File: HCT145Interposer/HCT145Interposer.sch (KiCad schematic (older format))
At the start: 8 parts, among them J1 Conn_01x01, J3 Header, J7 FORWARD, J8 REVERSE, U1 74HCT125, U2 74LVC245

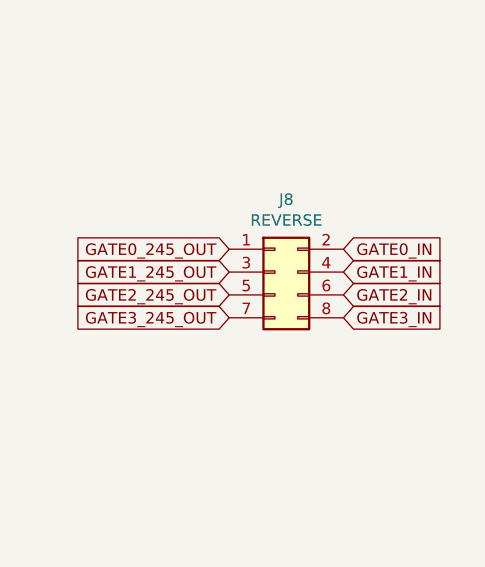
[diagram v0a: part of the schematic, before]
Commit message: Quick fix to HCT145 interposer. Reverse direction was outputting to wrong pins.
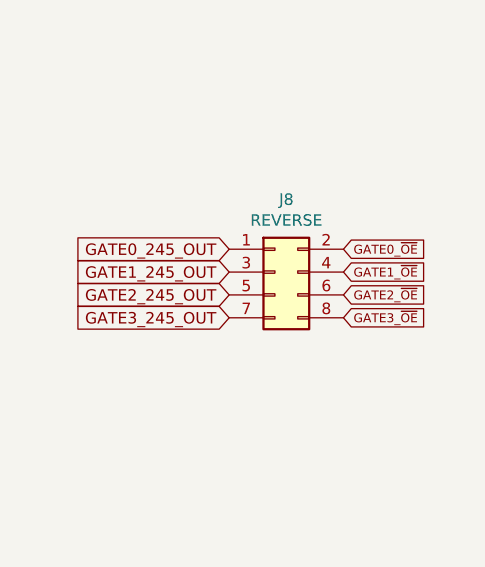
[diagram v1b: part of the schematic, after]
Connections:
- net GATE0_IN: no longer J8.2 (Pin_2)
- net GATE0_~OE: now also J8.2 (Pin_2)
- net GATE1_IN: no longer J8.4 (Pin_4)
- net GATE1_~OE: now also J8.4 (Pin_4)
- net GATE2_IN: no longer J8.6 (Pin_6)
- net GATE2_~OE: now also J8.6 (Pin_6)
- net GATE3_IN: no longer J8.8 (Pin_8)
- net GATE3_~OE: now also J8.8 (Pin_8)
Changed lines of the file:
@@
 Text GLabel 7600 4000 0    50   Input ~ 0
 GATE3_125_OUT
-Text GLabel 8350 1950 2    50   Input ~ 0
-GATE0_IN
-Text GLabel 8350 2050 2    50   Input ~ 0
-GATE1_IN
-Text GLabel 8350 2150 2    50   Input ~ 0
-GATE2_IN
-Text GLabel 8350 2250 2    50   Input ~ 0
-GATE3_IN
 Wire Wire Line
 	2650 2700 2550 2700
@@
 Connection ~ 2550 3000
 Connection ~ 2550 3300
+Text GLabel 8350 1950 2    39   Input ~ 0
+GATE0_~OE
+Text GLabel 8350 2050 2    39   Input ~ 0
+GATE1_~OE
+Text GLabel 8350 2150 2    39   Input ~ 0
+GATE2_~OE
+Text GLabel 8350 2250 2    39   Input ~ 0
+GATE3_~OE
 $EndSCHEMATC

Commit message: Udate HCT145 interposer. Much simplified (removes the HCT145) and laid out for planning breadboard construction.
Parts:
- removed C2: 0.1uF, Capacitor_THT:C_Disc_D6.0mm_W2.5mm_P5.00mm, symbol Device:C
- removed J7: FORWARD, Connector_PinHeader_2.54mm:PinHeader_2x04_P2.54mm_Vertical, symbol Connector_Generic:Conn_02x04_Odd_Even
- removed J8: REVERSE, Connector_PinHeader_2.54mm:PinHeader_2x04_P2.54mm_Vertical, symbol Connector_Generic:Conn_02x04_Odd_Even
- removed U1: 74HCT125, Package_DIP:DIP-14_W7.62mm_Socket, symbol 74xx:74LS125
- U1: renamed from U2; symbol 00Custom:74LS245_One_Way -> 00Custom:74LS245_One_Way_Reverse
- renumbered J3 to J1, J1 to J2
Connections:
- net GATE0_~OE is gone; now on net NEW_DRQ_OUT_3V3: J1.1 (Pin_1)
- net GATE3_245_OUT is gone; now on net NEW_IRQ_IN: U1.15 (B3)
- net +3V3: now also C1.1; no longer U1.1 (A->B)
- net +5V: no longer C1.1
- net GND: now also U1.1 (A->B), U1.3 (A1), U1.4 (A2)
- net GATE0_245_OUT renamed NEW_DRQ_IN
- net NEW_DRQ_IN: now also J1.3 (Pin_3)
- net GATE0_IN renamed TIED_TO_5V_1
- net GATE0_OUT renamed NEW_DRQ_OUT_3V3
- net NEW_DRQ_OUT_3V3: no longer J1.3 (Pin_3)
- net GATE1_245_OUT: no longer names the net of U1.17 (B1)
- net GATE1_IN renamed TIED_TO_5V_2
- net GATE1_OUT renamed NEW_IRQ_IN
- net NEW_IRQ_IN: no longer U1.3 (A1)
- net GATE1_~OE renamed NEW_IRQ_OUT_3V3
- net NEW_IRQ_OUT_3V3: now also U1.5 (A3)
- net GATE2_245_OUT: no longer names the net of U1.16 (B2)
- net GATE2_IN renamed TIED_TO_GND_1
- net GATE2_OUT renamed ~DRIVE_ACTIVE
- net ~DRIVE_ACTIVE: no longer U1.4 (A2)
- net GATE2_~OE renamed ~DRIVE_ACTIVE~_IN_3V3_1
- net ~DRIVE_ACTIVE~_IN_3V3_1: now also J1.11 (Pin_11)
- net GATE3_IN renamed TIED_TO_GND_2
- removed net GATE3_OUT: J1.11 (Pin_11), U1.5 (A3)
- net GATE3_~OE renamed ~DRIVE_ACTIVE~_IN_3V3_2
- no-connect marks 4 -> 12
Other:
- moved on the sheet: C1, U1
